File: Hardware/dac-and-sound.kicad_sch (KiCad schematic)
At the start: 6 parts, among them J3 AudioPlug3, U5 MCP4728T-E/UN

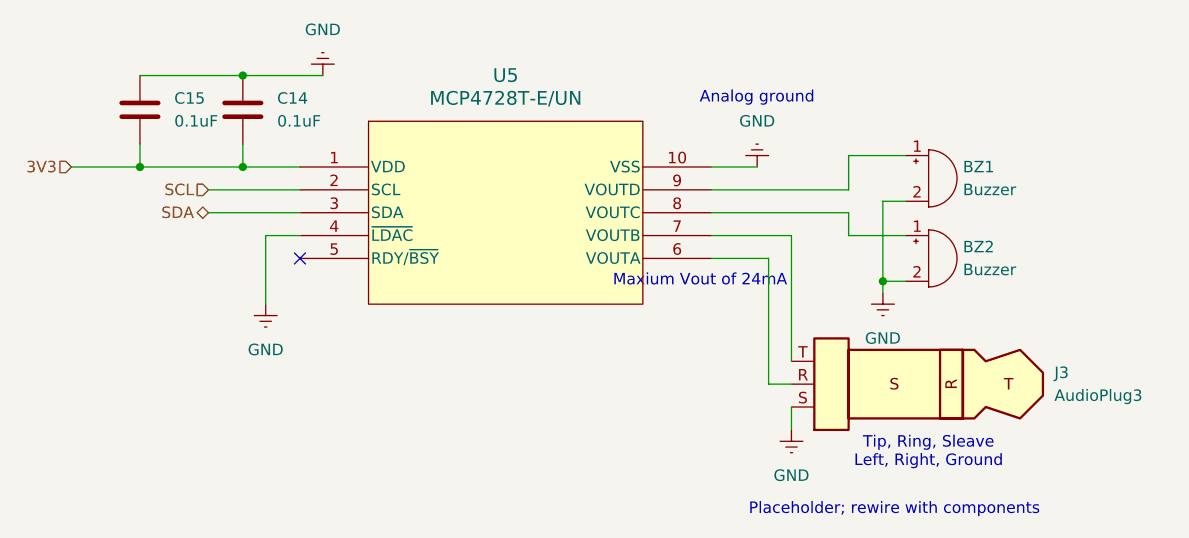
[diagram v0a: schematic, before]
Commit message: Add Battery Monitoring & Use Project Parts Library
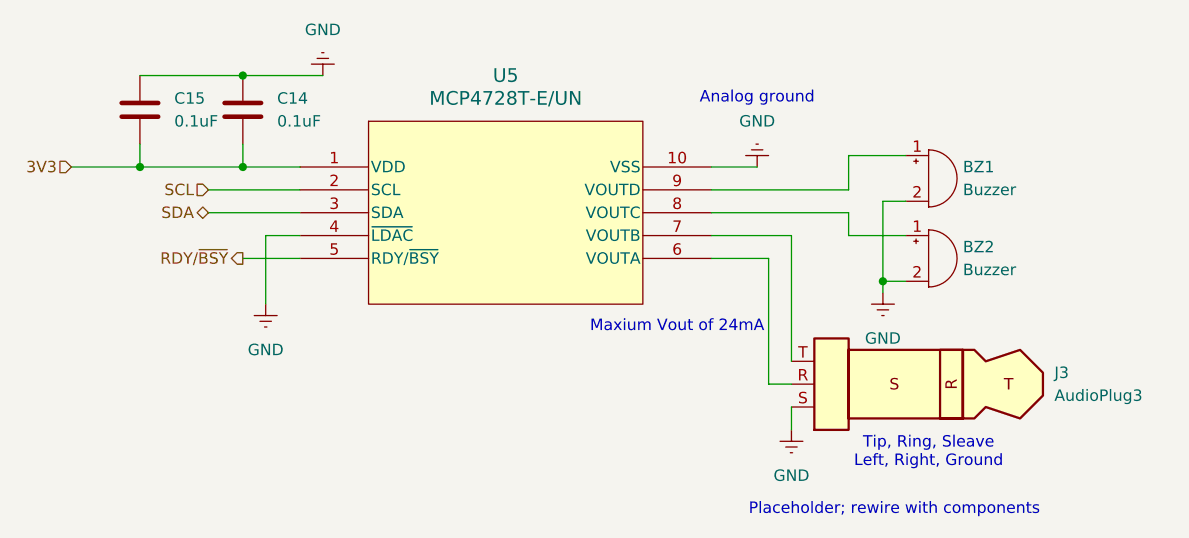
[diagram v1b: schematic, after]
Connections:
- net RDY/~{BSY}: now reaches U5.5 (RDY/~{BSY})
- no-connect marks 1 -> 0
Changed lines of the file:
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@@
 		(color 0 0 0 0)
 	)
-	(no_connect
-		(at 86.36 99.06)
-	)
 	(wire
 		(pts
@@
 	(wire
 		(pts
+			(xy 80.01 99.06) (xy 86.36 99.06)
+		)
+		(stroke
+			(width 0)
+			(type default)
+		)
+	)
+	(wire
+		(pts
 			(xy 147.32 96.52) (xy 147.32 93.98)
 		)
@@
 	(text "Maxium Vout of 24mA"
 		(exclude_from_sim no)
-		(at 130.81 101.6 0)
+		(at 128.27 106.68 0)
 		(effects
 			(font
@@
 		(shape input)
 		(at 60.96 88.9 180)
+		(fields_autoplaced yes)
+		(effects
+			(font
+				(size 1.27 1.27)
+			)
+			(justify right)
+		)
+	)
+	(hierarchical_label "RDY{slash}~{BSY}"
+		(shape output)
+		(at 80.01 99.06 180)
 		(fields_autoplaced yes)
 		(effects
@@
 			)
 		)
-		(property "Description" ""
+		(property "Description" "4-Channel DAC"
 			(at 86.36 88.9 0)
 			(effects

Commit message: Fully wired board!
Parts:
- C14, C15: footprint Capacitor_SMD:C_0201_0603Metric -> Resistor_SMD:R_01005_0402Metric; symbol Device:C -> Peanut:C
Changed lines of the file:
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@@
 	)
 	(symbol
-		(lib_id "Device:C")
+		(lib_id "Peanut:C")
 		(at 80.01 82.55 0)
 		(unit 1)
@@
 			)
 		)
-		(property "Footprint" "Capacitor_SMD:C_0201_0603Metric"
+		(property "Footprint" "Resistor_SMD:R_01005_0402Metric"
 			(at 80.9752 86.36 0)
 			(effects
@@
 	)
 	(symbol
-		(lib_id "Device:C")
+		(lib_id "Peanut:C")
 		(at 68.58 82.55 0)
 		(unit 1)
@@
 			)
 		)
-		(property "Footprint" "Capacitor_SMD:C_0201_0603Metric"
+		(property "Footprint" "Resistor_SMD:R_01005_0402Metric"
 			(at 69.5452 86.36 0)
 			(effects

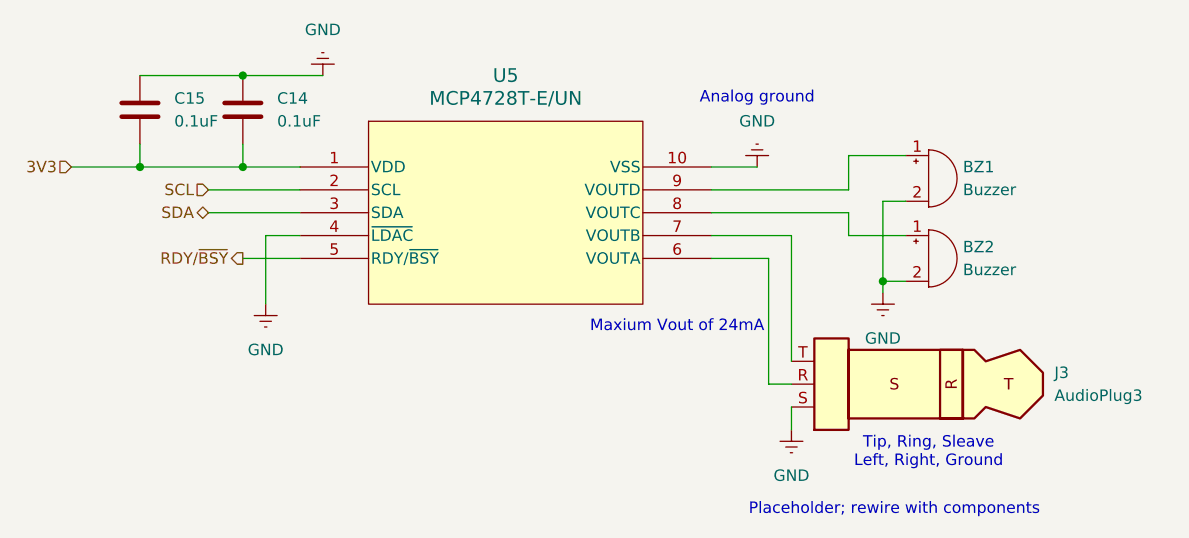
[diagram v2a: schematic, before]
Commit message: Initial OS architecture, and updated PCB work After a joint planning session, designed and architected OS structure: ``` src/ |- os: Audio, Accelerometer, Humidity, etc |- drivers: I2C interfaces, per-chip ```
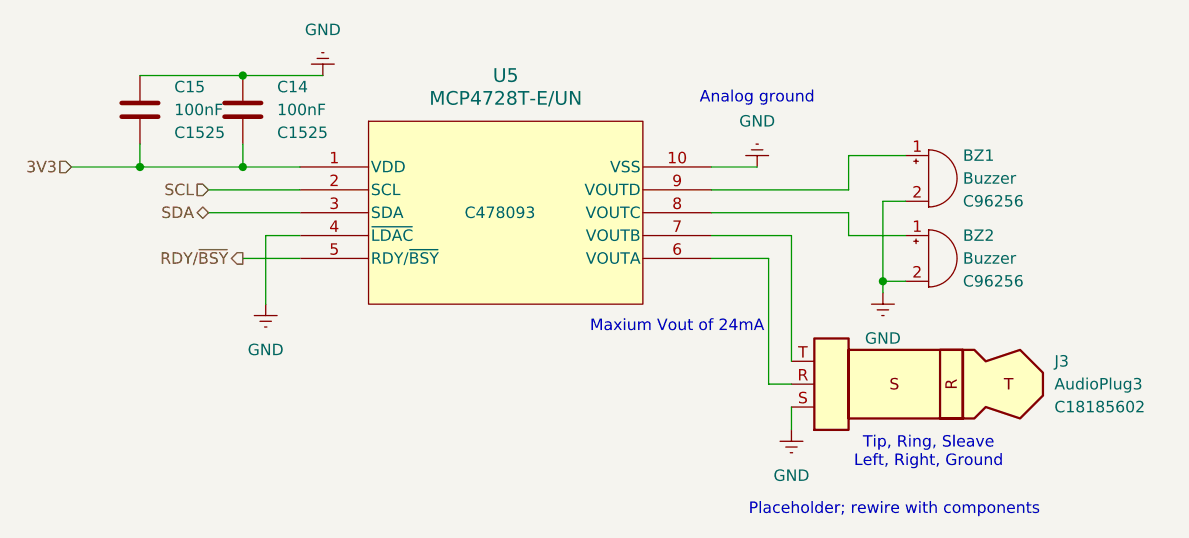
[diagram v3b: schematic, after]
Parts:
- BZ1, BZ2: symbol Device:Buzzer -> Peanut:QMB-09B-03; LCSC (none) -> C96256
- C14, C15: value 0.1uF -> 100nF; footprint Resistor_SMD:R_01005_0402Metric -> Capacitor_SMD:C_0402_1005Metric; symbol Peanut:C -> Peanut:C 100nF; LCSC (none) -> C1525
- J3: footprint Connector_Audio:Jack_3.5mm_CUI_SJ-3523-SMT_Horizontal -> Peanut:AUDIO-TH_PJ-320A-4P-DIP; symbol Connector_Audio:AudioPlug3 -> Peanut:PJ-320A-4P DIP; LCSC (none) -> C18185602
- U5: LCSC (none) -> C478093
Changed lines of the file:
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@@
 		(on_board yes)
 		(dnp no)
-		(fields_autoplaced yes)
 		(property "Reference" "U5"
 			(at 109.22 78.74 0)
@@
 			)
 		)
+		(property "LCSC" "C478093"
+			(at 108.585 93.98 0)
+			(effects
+				(font
+					(size 1.27 1.27)
+				)
+			)
+		)
 		(pin "10"
 		)
@@
 	)
 	(symbol
-		(lib_id "Peanut:C")
+		(lib_id "Peanut:C 100nF")
 		(at 80.01 82.55 0)
 		(unit 1)
@@
 		(fields_autoplaced yes)
 		(property "Reference" "C14"
-			(at 83.82 81.2799 0)
-			(effects
-				(font
-					(size 1.27 1.27)
-				)
-				(justify left)
-			)
-		)
-		(property "Value" "0.1uF"
-			(at 83.82 83.8199 0)
-			(effects
-				(font
-					(size 1.27 1.27)
-				)
-				(justify left)
-			)
-		)
-		(property "Footprint" "Resistor_SMD:R_01005_0402Metric"
+			(at 83.82 80.0099 0)
+			(effects
+				(font
+					(size 1.27 1.27)
+				)
+				(justify left)
+			)
+		)
+		(property "Value" "100nF"
+			(at 83.82 82.5499 0)
+			(effects
+				(font
+					(size 1.27 1.27)
+				)
+				(justify left)
+			)
+		)
+		(property "Footprint" "Capacitor_SMD:C_0402_1005Metric"
 			(at 80.9752 86.36 0)
 			(effects
@@
 			)
 		)
-		(property "Description" "Unpolarized capacitor"
+		(property "Description" "Capacitor 100nF"
 			(at 80.01 82.55 0)
 			(effects
@@
 			)
 		)
+		(property "LCSC" "C1525"
+			(at 83.82 85.0899 0)
+			(effects
+				(font
+					(size 1.27 1.27)
+				)
+				(justify left)
+			)
+		)
 		(pin "2"
 		)
@@
 	)
 	(symbol
-		(lib_id "Device:Buzzer")
+		(lib_id "Peanut:QMB-09B-03")
 		(at 156.21 90.17 0)
 		(unit 1)
@@
 		(fields_autoplaced yes)
 		(property "Reference" "BZ1"
-			(at 160.02 88.8999 0)
+			(at 160.02 87.6299 0)
 			(effects
 				(font
@@
 		)
 		(property "Value" "Buzzer"
-			(at 160.02 91.4399 0)
+			(at 160.02 90.1699 0)
 			(effects
 				(font
@@
 			)
 		)
+		(property "LCSC" "C96256"
+			(at 160.02 92.7099 0)
+			(effects
+				(font
+					(size 1.27 1.27)
+				)
+				(justify left)
+			)
+		)
 		(pin "1"
 		)
@@
 	)
 	(symbol
-		(lib_id "Peanut:C")
+		(lib_id "Peanut:C 100nF")
 		(at 68.58 82.55 0)
 		(unit 1)
@@
 		(fields_autoplaced yes)
 		(property "Reference" "C15"
-			(at 72.39 81.2799 0)
-			(effects
-				(font
-					(size 1.27 1.27)
-				)
-				(justify left)
-			)
-		)
-		(property "Value" "0.1uF"
-			(at 72.39 83.8199 0)
-			(effects
-				(font
-					(size 1.27 1.27)
-				)
-				(justify left)
-			)
-		)
-		(property "Footprint" "Resistor_SMD:R_01005_0402Metric"
+			(at 72.39 80.0099 0)
+			(effects
+				(font
+					(size 1.27 1.27)
+				)
+				(justify left)
+			)
+		)
+		(property "Value" "100nF"
+			(at 72.39 82.5499 0)
+			(effects
+				(font
+					(size 1.27 1.27)
+				)
+				(justify left)
+			)
+		)
+		(property "Footprint" "Capacitor_SMD:C_0402_1005Metric"
 			(at 69.5452 86.36 0)
 			(effects
@@
 			)
 		)
-		(property "Description" "Unpolarized capacitor"
+		(property "Description" "Capacitor 100nF"
 			(at 68.58 82.55 0)
 			(effects
@@
 				)
 				(hide yes)
+			)
+		)
+		(property "LCSC" "C1525"
+			(at 72.39 85.0899 0)
+			(effects
+				(font
+					(size 1.27 1.27)
+				)
+				(justify left)
 			)
 		)
@@
 	)
 	(symbol
-		(lib_id "Connector_Audio:AudioPlug3")
+		(lib_id "Peanut:PJ-320A-4P DIP")
 		(at 156.21 113.03 180)
 		(unit 1)
@@
 		(fields_autoplaced yes)
 		(property "Reference" "J3"
-			(at 170.18 111.7599 0)
+			(at 170.18 110.4899 0)
 			(effects
 				(font
@@
 		)
 		(property "Value" "AudioPlug3"
-			(at 170.18 114.2999 0)
+			(at 170.18 113.0299 0)
 			(effects
 				(font
@@
 			)
 		)
-		(property "Footprint" "Connector_Audio:Jack_3.5mm_CUI_SJ-3523-SMT_Horizontal"
+		(property "Footprint" "Peanut:AUDIO-TH_PJ-320A-4P-DIP"
 			(at 153.67 111.76 0)
 			(effects
@@
 			)
 		)
+		(property "LCSC" "C18185602"
+			(at 170.18 115.5699 0)
+			(effects
+				(font
+					(size 1.27 1.27)
+				)
+				(justify right)
+			)
+		)
 		(pin "T"
 		)
@@
 	)
 	(symbol
-		(lib_id "Device:Buzzer")
+		(lib_id "Peanut:QMB-09B-03")
 		(at 156.21 99.06 0)
 		(unit 1)
@@
 		(fields_autoplaced yes)
 		(property "Reference" "BZ2"
-			(at 160.02 97.7899 0)
+			(at 160.02 96.5199 0)
 			(effects
 				(font
@@
 		)
 		(property "Value" "Buzzer"
-			(at 160.02 100.3299 0)
+			(at 160.02 99.0599 0)
 			(effects
 				(font
@@
 			)
 		)
+		(property "LCSC" "C96256"
+			(at 160.02 101.5999 0)
+			(effects
+				(font
+					(size 1.27 1.27)
+				)
+				(justify left)
+			)
+		)

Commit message: Updates to PCB and ADC Schematics
- Swapped audio jack to correct pin (4P-DIP)
- Add LCSC numbers for all components
- Reroute some sensitive signal traces
- Add Board rev and author
- add 4x M2 mounting holes
- fixup some misc silkscreen, footprints, and component 3d models
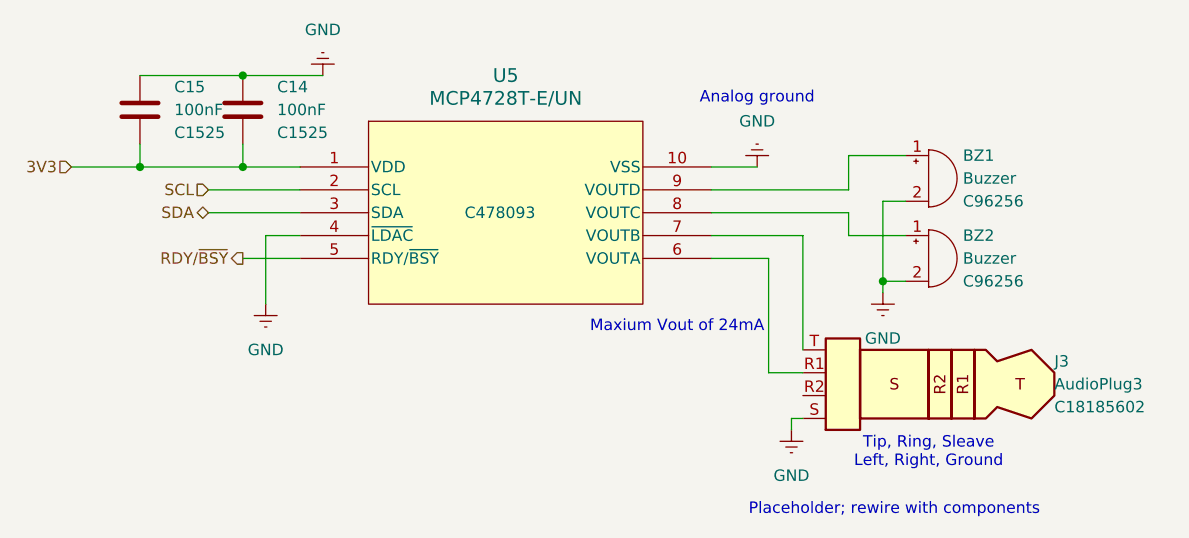
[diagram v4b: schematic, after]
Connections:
- net at U5.6 (VOUTA): now also J3.R1; no longer J3.R
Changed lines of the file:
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@@
 	(wire
 		(pts
-			(xy 140.97 115.57) (xy 140.97 118.11)
+			(xy 142.24 111.76) (xy 138.43 111.76)
 		)
 		(stroke
@@
 	(wire
 		(pts
-			(xy 140.97 96.52) (xy 140.97 110.49)
-		)
-		(stroke
-			(width 0)
-			(type default)
-		)
-	)
-	(wire
-		(pts
 			(xy 147.32 87.63) (xy 153.67 87.63)
 		)
@@
 	(wire
 		(pts
-			(xy 138.43 113.03) (xy 140.97 113.03)
+			(xy 140.97 116.84) (xy 140.97 118.11)
+		)
+		(stroke
+			(width 0)
+			(type default)
+		)
+	)
+	(wire
+		(pts
+			(xy 142.24 96.52) (xy 142.24 109.22)
+		)
+		(stroke
+			(width 0)
+			(type default)
+		)
+	)
+	(wire
+		(pts
+			(xy 138.43 111.76) (xy 138.43 99.06)
 		)
 		(stroke
@@
 	(wire
 		(pts
+			(xy 142.24 116.84) (xy 140.97 116.84)
+		)
+		(stroke
+			(width 0)
+			(type default)
+		)
+	)
+	(wire
+		(pts
 			(xy 153.67 96.52) (xy 147.32 96.52)
 		)
@@
 	(wire
 		(pts
-			(xy 138.43 99.06) (xy 138.43 113.03)
-		)
-		(stroke
-			(width 0)
-			(type default)
-		)
-	)
-	(wire
-		(pts
 			(xy 151.13 101.6) (xy 151.13 92.71)
 		)
@@
 	(wire
 		(pts
-			(xy 132.08 96.52) (xy 140.97 96.52)
+			(xy 132.08 96.52) (xy 142.24 96.52)
 		)
 		(stroke
@@
 		(pin "T"
 		)
-		(pin "R"
+		(pin "R1"
 		)
 		(pin "S"
 		)
+		(pin "R2"
+		)
 		(instances
